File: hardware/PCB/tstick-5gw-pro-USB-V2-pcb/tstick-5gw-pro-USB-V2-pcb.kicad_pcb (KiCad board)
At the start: 4 copper layers, 55.9 x 25.4 mm, 62 parts, among them J1 USB_C_Receptacle_USB2.0, Q1 BSS138, Q2 BSS138, Q3 BSS138, SW1 JST-SH-1.00mm 1x2, SW2 PTS810 SJM Switch, SW3 PTS810 SJM Switch, U2 MCP73871, U3 NCP167AMX330TBG, U4 NCP167AMX180TBG

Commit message: added updated bill of materials and manufacturing files
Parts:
- removed D2: ESD5Zxx, Diode_SMD:D_SOD-523
- added C15: 0.1uF, Capacitor_SMD:C_0201_0603Metric, F.Cu at (106.1, 62.1)
- added U1: USBLC6-2P6, Package_TO_SOT_SMD:SOT-666, F.Cu at (103.9, 61.9)
- TrillExtensionInput1: value JST-SH 1x08 1.00mm -> JST-SH-1x04 1.0mm
- moved CHARGLED1 2.73 mm to (105.5, 70.8), turned to 180 degrees
- moved C3 1.91 mm to (105.0, 63.6)
- moved CHARGLED2 1.66 mm to (105.5, 69.8), turned to 180 degrees
- moved R7 1.47 mm to (102.9, 58.0)
- moved C14 1.41 mm to (103.4, 66.6)
- moved CHARGLED3 1.31 mm to (105.5, 68.9), turned to 180 degrees
- moved R4 1.21 mm to (105.0, 65.1)
- moved R18 1.16 mm to (105.0, 64.3)
- moved TH2 1.12 mm to (104.9, 67.4)
- moved U2 0.79 mm to (108.3, 65.8)
- moved R22 0.78 mm to (107.5, 69.1)
- moved R24 0.78 mm to (106.8, 69.1)
- moved R3 0.78 mm to (108.3, 69.1)
- moved R6 0.69 mm to (103.2, 63.7)
- moved R2 0.39 mm to (107.6, 60.1)
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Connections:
- J1 pad A6: /USBD+ -> /D+
- J1 pad A7: /USBD- -> /D-
- J1 pad B6: /USBD+ -> /D+
- J1 pad B7: /USBD- -> /D-
- U2 pad 17: SYS -> VUSB
- U2 pad 3: GND -> VUSB
- U2 pad 4: SYS -> VUSB
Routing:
- net /USBD-: track 42.2 -> 35.6 mm
- net /USBD+: track 39.4 -> 34.1 mm
- net /D-: track 0.00 -> 4.93 mm
- net GND: track 95.5 -> 90.5 mm, vias 58 -> 57
- net /D+: track 0.00 -> 4.20 mm
- net VUSB: track 13.2 -> 17.2 mm, vias 6 -> 9
- net +BATT: track 7.97 -> 10.6 mm, vias 6 -> 7
- net Net-(CHARGLED1-K): track 1.02 -> 2.92 mm
- net Net-(CHARGLED2-K): track 1.10 -> 1.77 mm
- net SYS: track 8.89 -> 8.75 mm, vias 8 -> 5

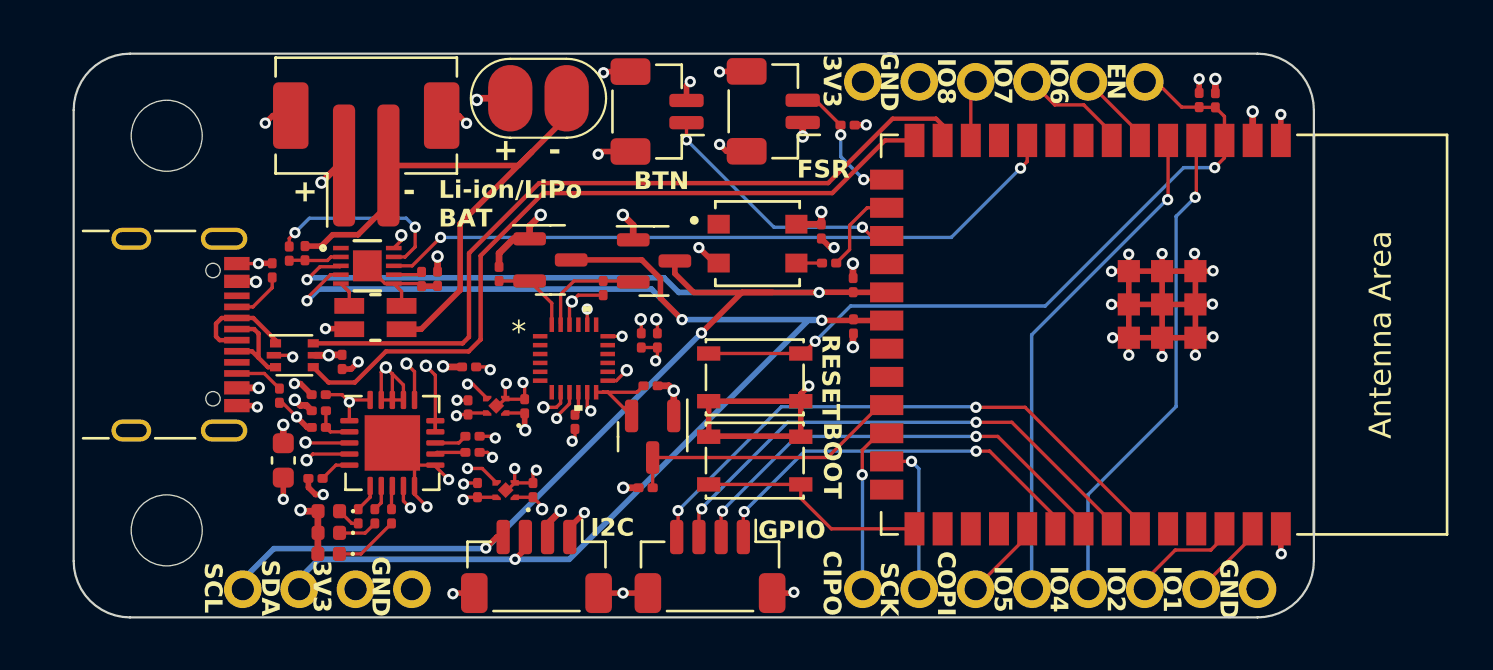
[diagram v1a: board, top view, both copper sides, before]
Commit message: added fully flexible pcb for the touch sensor
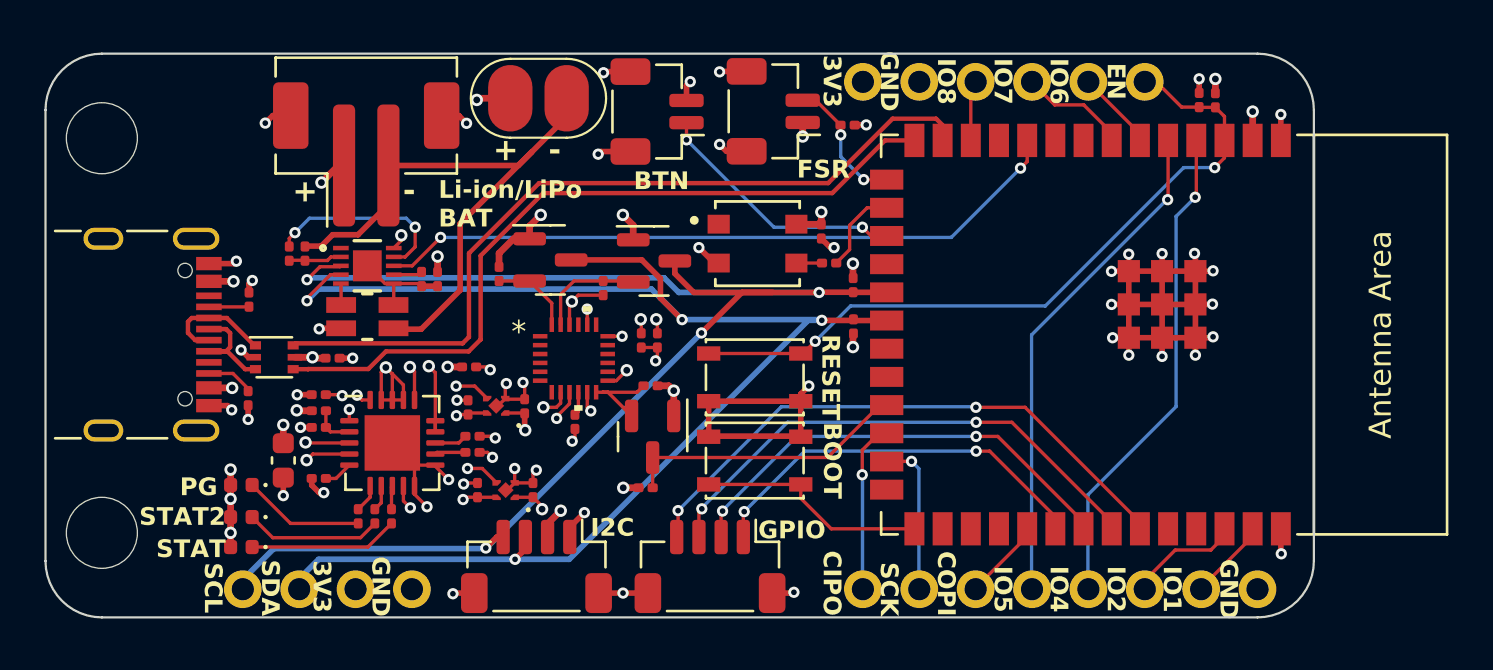
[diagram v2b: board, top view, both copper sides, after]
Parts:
- moved CHARGLED3 4.11 mm to (101.5, 67.7)
- moved CHARGLED2 4.00 mm to (101.5, 69.1)
- moved CHARGLED1 3.94 mm to (101.5, 70.5)
- moved H1 2.92 mm to (95.2, 52.1)
- moved H2 2.92 mm to (95.2, 69.8)
- moved R7 1.68 mm to (101.9, 59.3)
- moved R6 1.41 mm to (101.8, 63.8)
- moved J1 1.26 mm to (96.4, 60.9)
- moved U1 0.91 mm to (103.0, 61.9)
- moved C15 0.46 mm to (105.6, 62.0), turned to 0 degrees
- moved R2 0.37 mm to (107.2, 60.1)
- moved TH2 0.15 mm to (105.0, 67.4)
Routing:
- net Net-(CHARGLED3-K): track 1.07 -> 5.50 mm
- net Net-(CHARGLED2-K): track 1.77 -> 6.18 mm
- net Net-(CHARGLED1-K): track 2.92 -> 6.72 mm
- net GND: track 90.5 -> 89.1 mm, vias 57 -> 59
- net /D+: track 4.20 -> 5.14 mm
- net /USBD-: track 35.6 -> 36.5 mm
- net VUSB: track 17.2 -> 18.0 mm, vias 9 -> 11
- net Net-(J1-CC1): track 2.41 -> 1.81 mm
- net SYS: track 8.75 -> 8.15 mm, vias 5 -> 7
- net +BATT: track 10.6 -> 10.1 mm
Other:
- board size 55.9 x 25.4 mm -> 57.2 x 25.4 mm
- board text added: "2 pin JST-PH Horizontal Header"
- board text added: "2 pin JST-SH Horizontal Header"
- board text added: "4 pin JST-SH Horizontal Header"
- board text added: "Boot Button"
- board text added: "ESP32-S3 WROOM 2"
- board text added: "Fuel Gauge"
- board text added: "ICM20948"
- board text added: "Indicator LEDs (RED)"
- board text added: "MCP73871"
- board text added: "NCP167AMX 180TBG"
- board text added: "NCP167AMX 330TBG"
- board text added: "Neopixel"
- board text added: "Ohmite LVK12 Shunt Resistor"
- board text added: "PG"
- board text added: "Reset Button"
- board text added: "STAT"
- board text added: "STAT2"
- board text added: "USB C Receptacle"
- board text added: "USBLC6-LP6"

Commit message: added up to date manufacturing files
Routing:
- net GND: track 89.1 -> 87.0 mm
- net /IO4: track 21.9 -> 23.1 mm

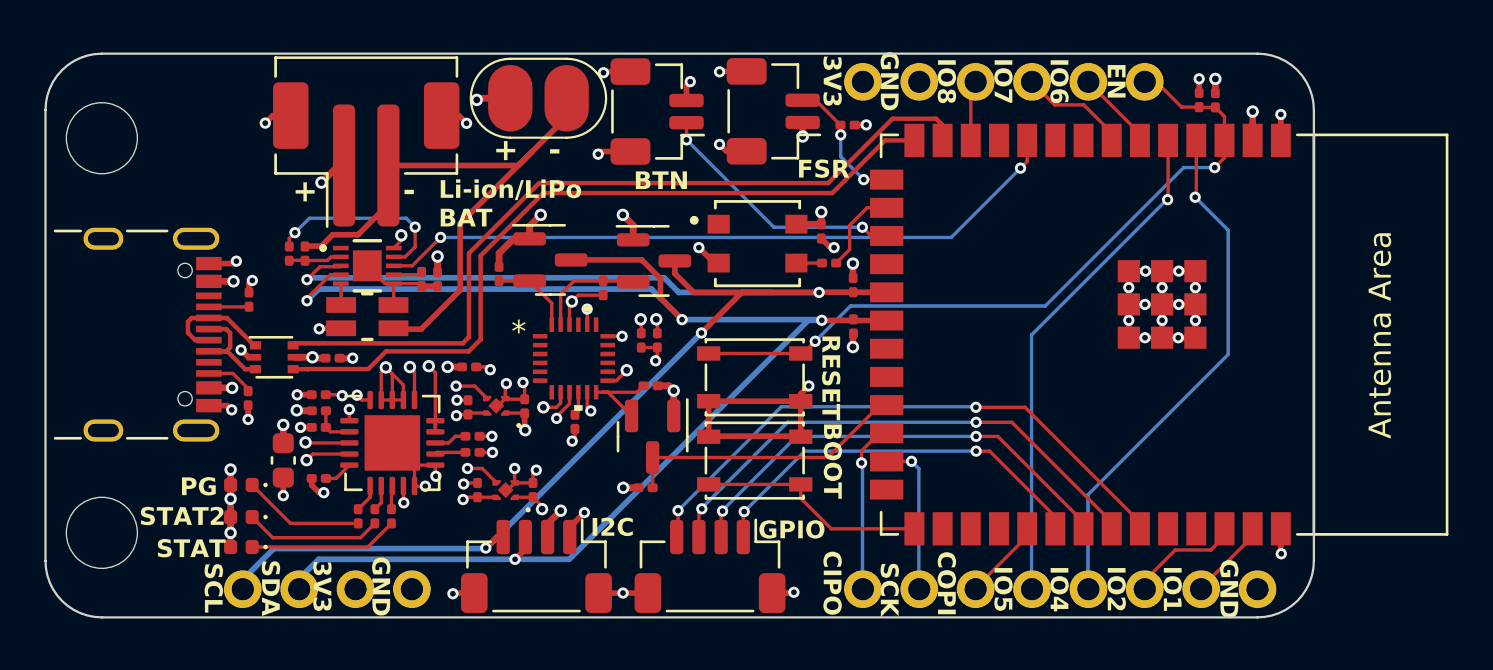
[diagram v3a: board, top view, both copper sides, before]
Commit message: reduced size of esp32 pcb to 1x2.35 inch, used ssmaller neopixel, updated BOM
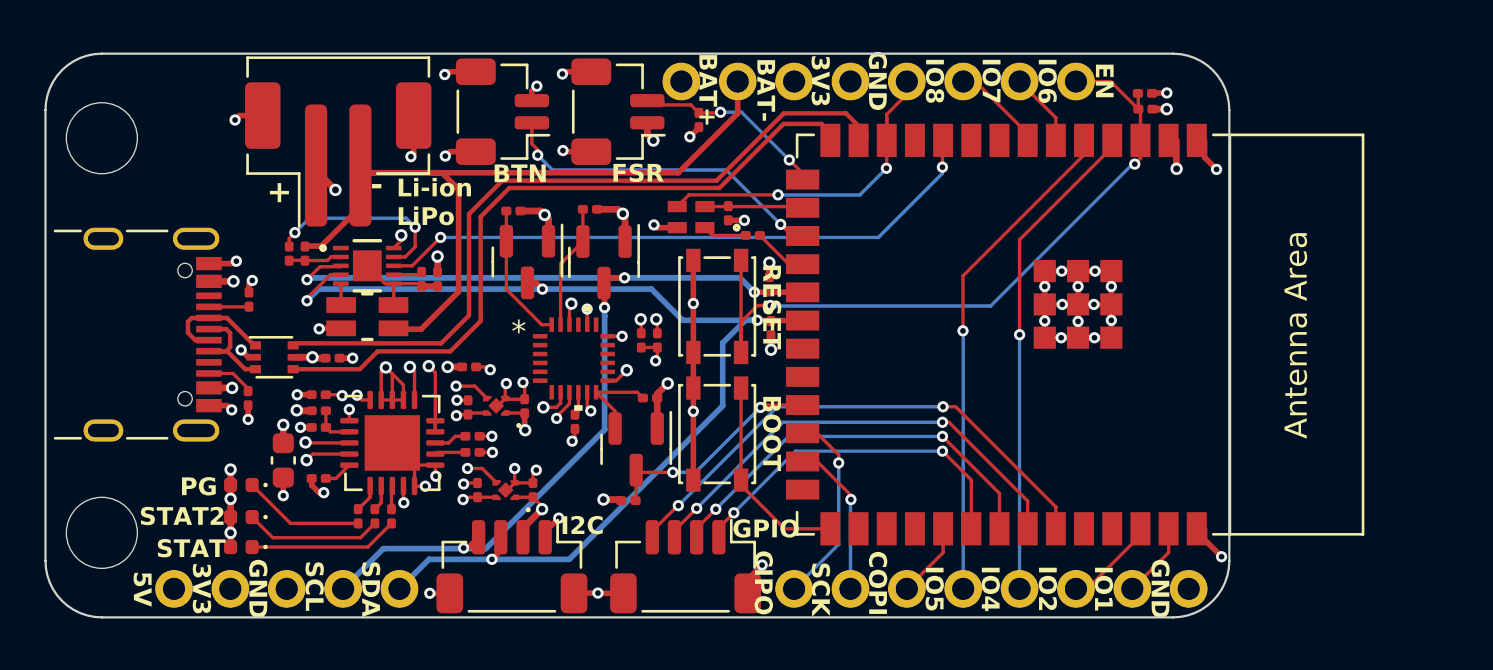
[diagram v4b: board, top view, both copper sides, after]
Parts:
- removed BT2: Battery_Cell, solderpads:SolderPad
- removed R13: 300, Resistor_SMD:R_0201_0603Metric
- added R8: 300, Resistor_SMD:R_0201_0603Metric, F.Cu at (124.6, 56.5)
- PWLED1: value SK6812MINI -> SK6805-E-J; footprint neopixel:2659 -> neopixel-1515-footprints:4492_ADA
- moved FSR1 7.00 mm to (118.5, 50.9)
- moved SW1 6.97 mm to (113.3, 50.9)
- moved R1 6.71 mm to (122.2, 51.2), turned to -90 degrees
- moved C13 4.27 mm to (123.5, 55.5)
- moved MCU1 3.79 mm to (136.3, 60.9)
- moved R19 3.78 mm to (125.3, 58.6)
- moved R16 3.72 mm to (125.4, 60.6)
- moved SW3 3.61 mm to (123.0, 59.6), turned to -90 degrees
- moved R14 3.60 mm to (117.2, 55.3), turned to 0 degrees
- moved PWLED1 3.22 mm to (121.8, 55.6), turned to 180 degrees
- moved R5 3.18 mm to (142.3, 50.8), turned to 0 degrees
- moved BOARDLAYOUT1 3.10 mm to (131.5, 49.5)
- moved R15 2.91 mm to (113.8, 55.4), turned to 0 degrees
- moved C9 2.46 mm to (142.2, 50.0), turned to 0 degrees
- moved Q1 2.26 mm to (117.9, 57.7), turned to -90 degrees
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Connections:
- BOARDLAYOUT1 pad 1: +3V3 -> +BATT
- BOARDLAYOUT1 pad 10: /IO4 -> /IO1
- BOARDLAYOUT1 pad 11: /IO5 -> /IO2
- BOARDLAYOUT1 pad 12: /COPI -> /IO4
- BOARDLAYOUT1 pad 13: /SCK -> /IO5
- BOARDLAYOUT1 pad 14: /CIPO -> /COPI
- BOARDLAYOUT1 pad 15: GND -> /SCK
- BOARDLAYOUT1 pad 16: +3V3 -> /CIPO
- BOARDLAYOUT1 pad 2: GND -> -BATT
- BOARDLAYOUT1 pad 3: /IO8 -> +3V3
- BOARDLAYOUT1 pad 4: /IO7 -> GND
- BOARDLAYOUT1 pad 5: /IO6 -> /IO8
- BOARDLAYOUT1 pad 6: /EN -> /IO7
- BOARDLAYOUT1 pad 7: GND -> /IO6
- BOARDLAYOUT1 pad 8: /IO1 -> /EN
- BOARDLAYOUT1 pad 9: /IO2 -> GND
- C13 pad 1: +3V3 -> /IO46
- PWLED1 pad 1: unconnected-(PWLED1-DOUT-Pad1) -> Net-(PWLED1-DIN)
- PWLED1 pad 2: GND -> /IO46
- PWLED1 pad 3: Net-(PWLED1-DIN) -> /IO8
- PWLED1 pad 4: +3V3 -> GND
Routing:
- net /SCL: track 65.8 -> 48.0 mm, vias 4 -> 5
- net /SDA: track 65.3 -> 50.3 mm
- net /IO8: track 2.72 -> 15.6 mm, vias 0 -> 2
- net GND: track 87.0 -> 76.7 mm, vias 59 -> 60
- net -BATT: track 27.0 -> 37.1 mm
- net /IO10: track 0.00 -> 3.78 mm
- net /IO9: track 11.6 -> 15.4 mm
- net /IO17: track 31.4 -> 28.1 mm
- net /USBD-: track 36.5 -> 33.5 mm
- net /IO41: track 23.6 -> 20.6 mm
- net /IO3: track 6.09 -> 8.99 mm
- net /IO40: track 20.8 -> 18.1 mm
- net /IO42: track 26.4 -> 23.8 mm
- net /LV_SDA: track 3.76 -> 6.23 mm
- net /IO21: track 12.9 -> 10.5 mm, vias 0 -> 2
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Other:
- board size 57.2 x 25.4 mm -> 53.3 x 25.4 mm
- board text added: "Li-ion LiPo"
- board text added: "SCL = IO11 SDA = IO12 LED DATA = IO10 LED EXTRA = IO08 LED POWER = IO46 IMU INT = IO21 FUEL GAUGE INT = IO17"
- board text removed: "3V3"
- board text removed: "GND"
- board text removed: "Li-ion/LiPo BAT"
- board text removed: "SCL = IO11 SDA = IO12 STATUS LED = IO46 IMU INT = IO21 FUEL GAUGE INT = IO17"

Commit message: updated BOM, cleaned up esp32 and touch board schematic (removed unused fields)
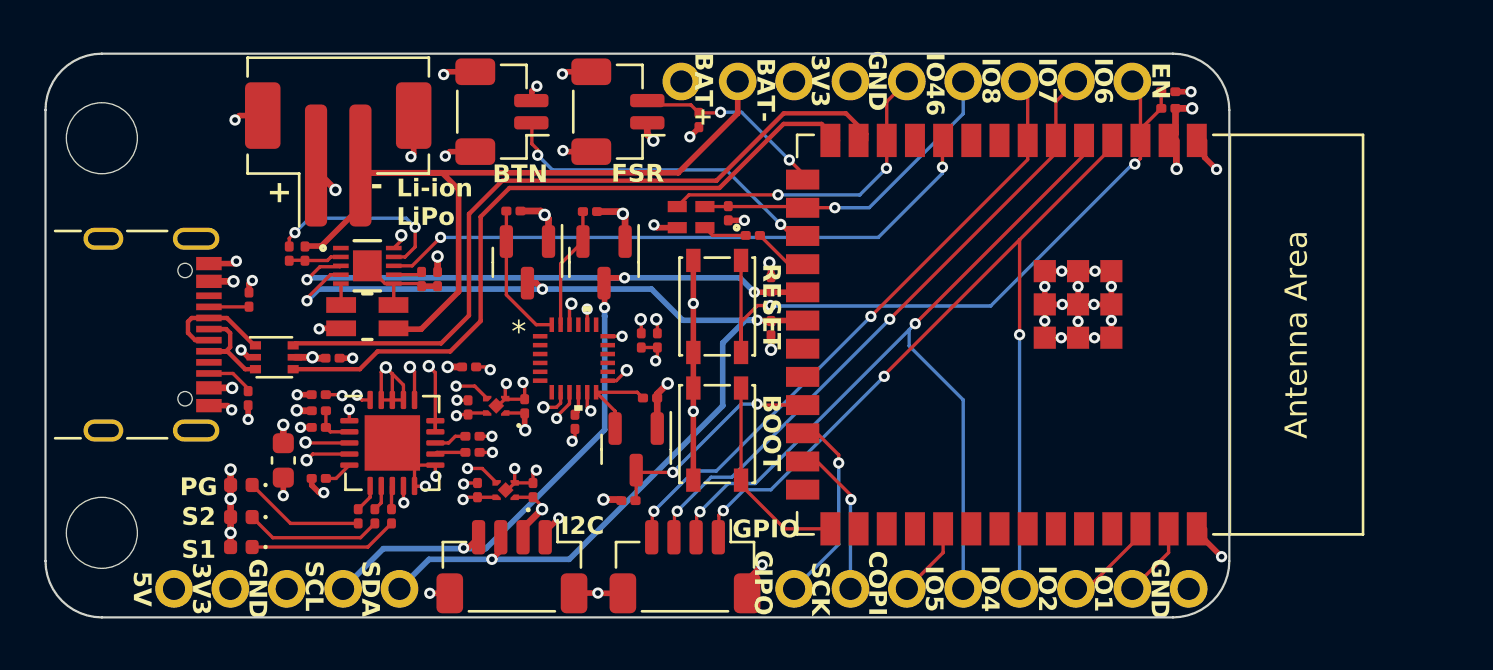
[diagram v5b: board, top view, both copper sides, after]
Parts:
- removed FSR1: JST-SH-1.00mm 1x2, Connector_JST:JST_SH_BM02B-SRSS-TB_1x02-1MP_P1.00mm_Vertical
- removed QWIIC1, TrillExtensionInput1: JST-SH-1x04 1.0mm, Connector_JST:JST_SH_BM04B-SRSS-TB_1x04-1MP_P1.00mm_Vertical
- removed SW3: PTS810 SJM Switch, Button_Switch_SMD:SW_SPST_PTS810
- added ANG1: JST-SH-1.00mm 1x2, Connector_JST:JST_SH_BM02B-SRSS-TB_1x02-1MP_P1.00mm_Vertical, F.Cu at (118.5, 50.9)
- added ANG2: JST-SH-1.00mm 1x2, Connector_JST:JST_SH_BM02B-SRSS-TB_1x02-1MP_P1.00mm_Vertical, F.Cu at (113.3, 50.9)
- added TOUCH1: JST-SH-1x04 1.0mm, Connector_JST:JST_SH_BM04B-SRSS-TB_1x04-1MP_P1.00mm_Vertical, F.Cu at (113.7, 71.4)
- added TOUCH2: JST-SH-1x04 1.0mm, Connector_JST:JST_SH_BM04B-SRSS-TB_1x04-1MP_P1.00mm_Vertical, F.Cu at (121.5, 71.4)
- SW1: value JST-SH-1.00mm 1x2 -> PTS810 SJM Switch; footprint Connector_JST:JST_SH_BM02B-SRSS-TB_1x02-1MP_P1.00mm_Vertical -> Button_Switch_SMD:SW_SPST_PTS810
- moved SW1 17.5 mm to (123.0, 65.4), turned to -90 degrees
- moved SW2 5.75 mm to (123.0, 59.6)
- moved C9 1.05 mm to (143.3, 50.0)
- moved R5 1.04 mm to (143.3, 50.7)
- moved R14 0.10 mm to (117.2, 55.4)
- moved R19 0.08 mm to (125.4, 58.6)
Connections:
- BOARDLAYOUT1 pad 10: /IO1 -> GND
- BOARDLAYOUT1 pad 11: /IO2 -> /IO1
- BOARDLAYOUT1 pad 12: /IO4 -> /IO2
- BOARDLAYOUT1 pad 13: /IO5 -> /IO4
- BOARDLAYOUT1 pad 14: /COPI -> /IO5
- BOARDLAYOUT1 pad 15: /SCK -> /COPI
- BOARDLAYOUT1 pad 16: /CIPO -> /SCK
- BOARDLAYOUT1 pad 17: /SDA -> /CIPO
- BOARDLAYOUT1 pad 18: /SCL -> /SDA
- BOARDLAYOUT1 pad 19: GND -> /SCL
- BOARDLAYOUT1 pad 20: +3V3 -> GND
- BOARDLAYOUT1 pad 21: VUSB -> +3V3
- BOARDLAYOUT1 pad 6: /IO7 -> /IO46
- BOARDLAYOUT1 pad 7: /IO6 -> /IO7
- BOARDLAYOUT1 pad 8: /EN -> /IO6
- BOARDLAYOUT1 pad 9: GND -> /EN
- SW1 pad 1: /IO9 -> /IO0
- SW2 pad 1: /IO0 -> /EN
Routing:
- net /IO6: track 3.33 -> 28.6 mm, vias 0 -> 2
- net /IO7: track 4.18 -> 28.3 mm, vias 0 -> 2
- net /IO42: track 23.8 -> 0.00 mm, vias 2 -> 0
- net /IO41: track 20.6 -> 0.00 mm, vias 2 -> 0
- net /IO4: track 21.9 -> 41.7 mm, vias 1 -> 3
- net /IO40: track 18.1 -> 0.00 mm, vias 2 -> 0
- net /IO5: track 22.5 -> 38.5 mm, vias 1 -> 2
- net /IO39: track 16.0 -> 0.00 mm, vias 2 -> 0
- net /IO46: track 4.70 -> 15.1 mm, vias 0 -> 1
- net +3V3: track 8.12 -> 9.83 mm
- net /IO8: track 15.6 -> 14.4 mm
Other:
- board text added: "1.8V"
- board text added: "2 pin JST-PH Vertical Header"
- board text added: "2 pin JST-SH Vertical Header"
- board text added: "3.3V"
- board text added: "4 pin JST-SH Vertical Header"
- board text added: "5V"
- board text added: "BAT+"
- board text added: "EVT1 = IO7 EVT2 = IO6 EVT3 = IO5 EVT4 = IO4"
- board text added: "S1"
- board text added: "S2"
- board text added: "SYS"
- board text removed: "2 pin JST-PH Horizontal Header"
- board text removed: "2 pin JST-SH Horizontal Header"
- board text removed: "4 pin JST-SH Horizontal Header"
- board text removed: "EVT1 = IO42 EVT2 = IO41 EVT3 = IO40 EVT4 = IO39"
- board text removed: "STAT"
- board text removed: "STAT2"
